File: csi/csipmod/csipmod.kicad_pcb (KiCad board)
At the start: 2 copper layers, 48 x 50 mm, 38 parts, among them J1 PMOD_1A, J2 PMOD_1B, P1 PICAM, U1 LD3985M18R_SOT23, U2 PCA9306

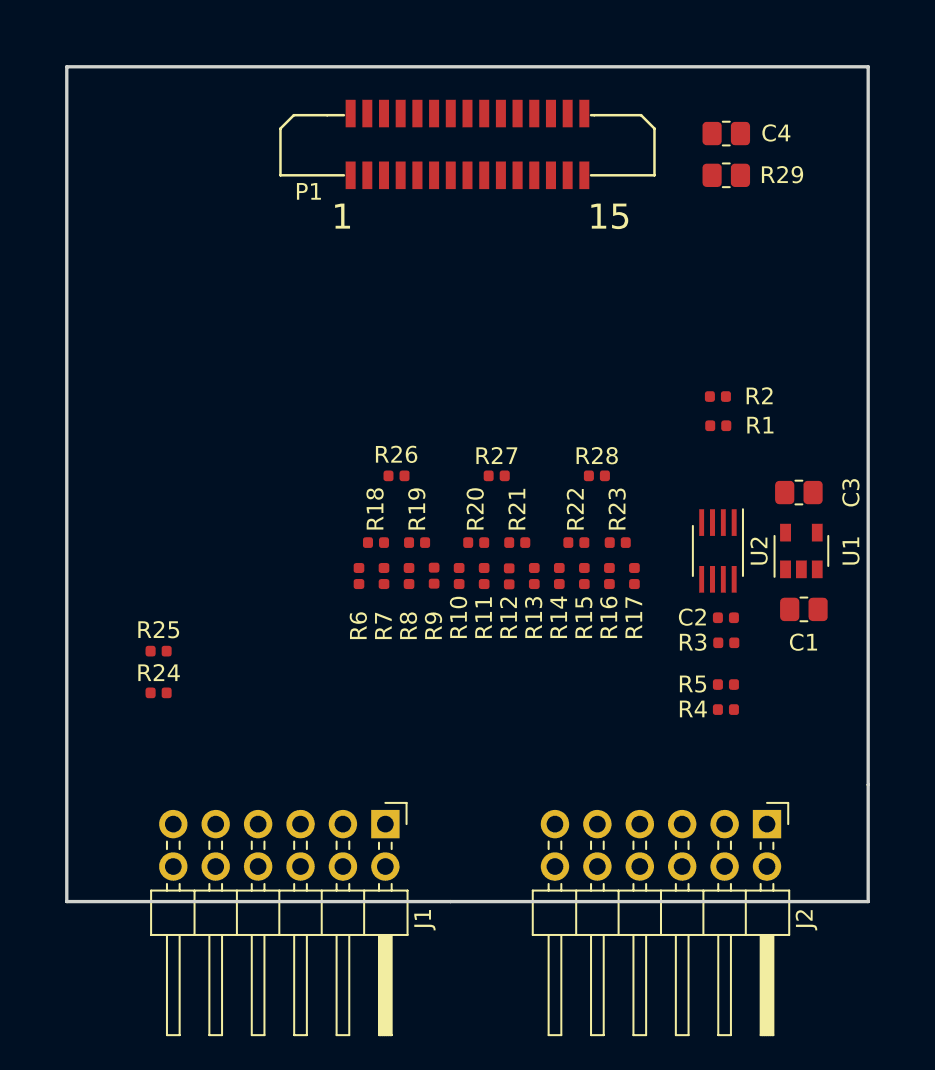
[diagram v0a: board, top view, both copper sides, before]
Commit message: csipmod: Routed
Signed-off-by: David Shah <davey1576@gmail.com>
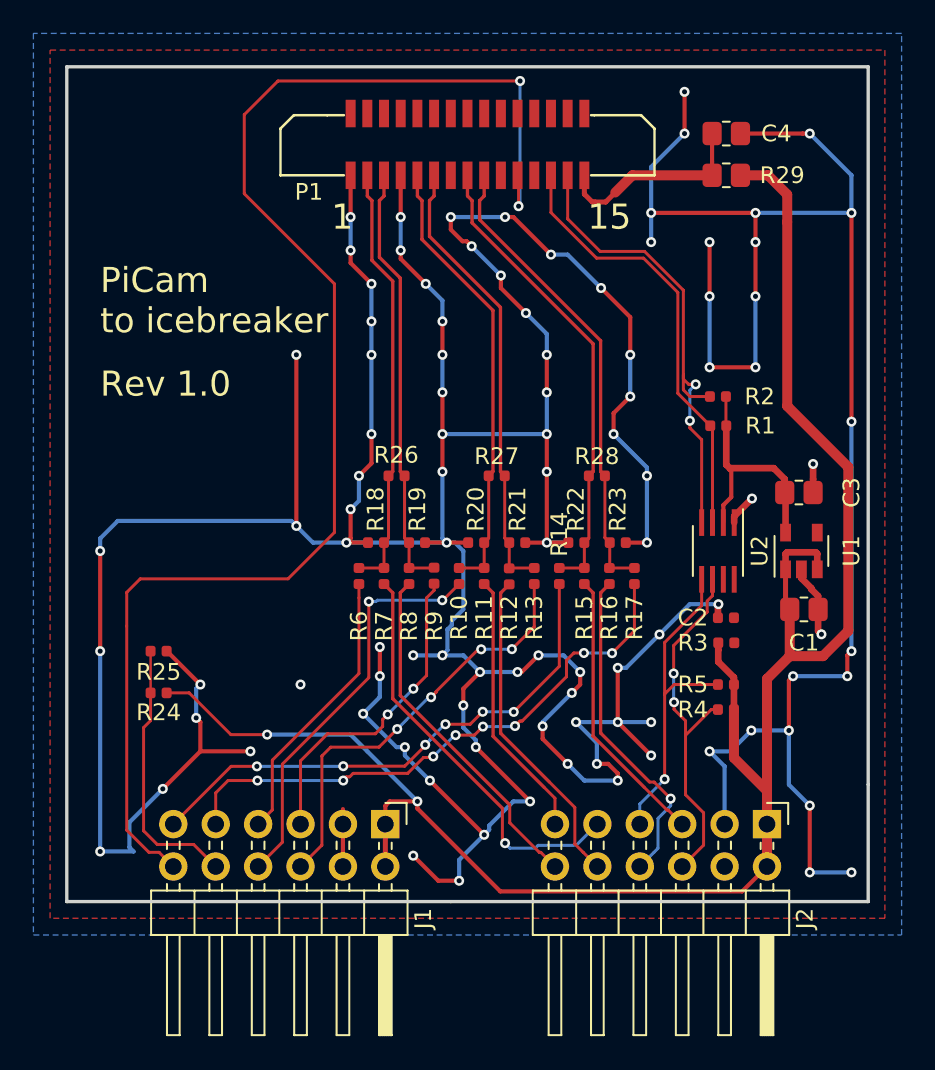
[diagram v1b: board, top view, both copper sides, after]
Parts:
- turned R14 to 270 degrees
- turned R24 to 180 degrees
- turned R25 to 0 degrees
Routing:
- net GND: track 0.00 -> 404.0 mm, vias 0 -> 100
- net +3V3: track 0.00 -> 115.3 mm, vias 0 -> 2
- net /CAM_ENABLE: track 0.00 -> 85.9 mm, vias 0 -> 2
- net /LPCLK+: track 0.00 -> 34.4 mm, vias 0 -> 8
- net /LPCLK-: track 0.00 -> 32.0 mm, vias 0 -> 6
- net /CAM_SDA: track 0.00 -> 28.9 mm, vias 0 -> 2
- net /CCLK+: track 0.00 -> 28.4 mm
- net /CCLK-: track 0.00 -> 28.4 mm
- net /CD1+: track 0.00 -> 27.1 mm
- net /CD1-: track 0.00 -> 27.1 mm
- net /CAM_SCL: track 0.00 -> 26.5 mm
- net /CD0+: track 0.00 -> 25.9 mm
- net /CD0-: track 0.00 -> 25.9 mm
- net /LPD1+: track 0.00 -> 25.7 mm, vias 0 -> 4
- net /HSD0-: track 0.00 -> 24.8 mm, vias 0 -> 1
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- added copper zone on B.Cu, net GND
- added copper zone on F.Cu, net GND
- added copper zone on In1.Cu, net GND
- added copper zone on In2.Cu, net GND
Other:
- copper layers 2 -> 4
- net class Default: clearance 0.2 -> 0.15; trace_width 0.25 -> 0.15; via_dia 0.8 -> 0.6; via_drill 0.4 -> 0.3
- rule trace_clearance: 0.2 -> 0.15
- rule trace_min: 0.2 -> 0.15
- rule via_min_size: 0.4 -> 0.16
- board text added: "PiCam to icebreaker"
- board text added: "Rev 1.0"

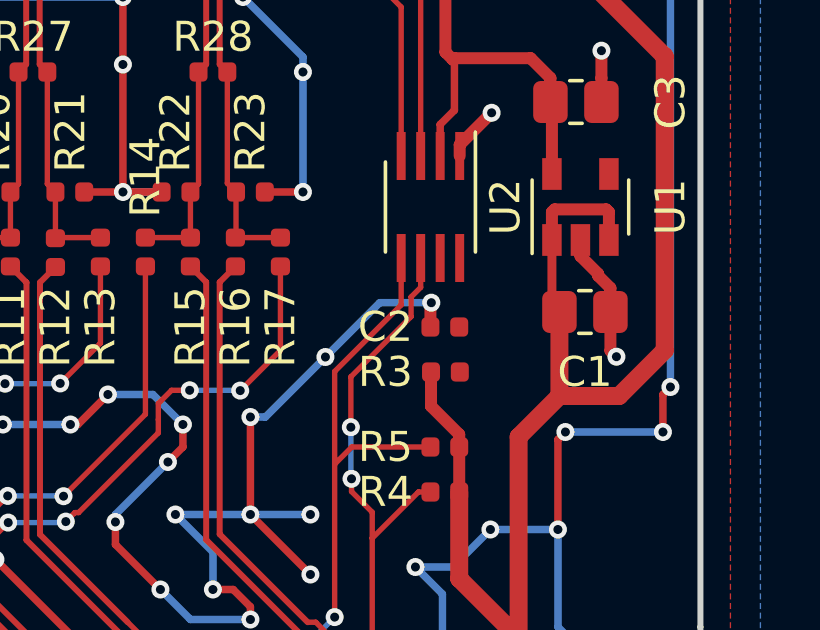
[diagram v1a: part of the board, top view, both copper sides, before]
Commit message: Adding CSI schematic and gerbers
Signed-off-by: David Shah <davey1576@gmail.com>
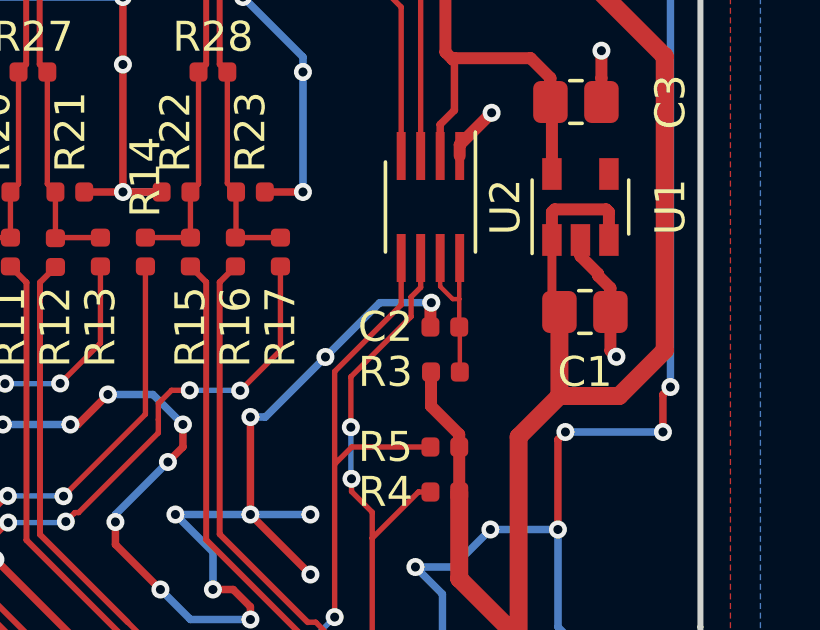
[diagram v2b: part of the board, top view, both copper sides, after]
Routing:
- net Net-(C2-Pad1): track 0.00 -> 5.57 mm
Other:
- rule pad_to_mask_clearance: 0.2 -> 0
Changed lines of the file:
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@@
     (thickness 1.6)
     (drawings 10)
-    (tracks 658)
+    (tracks 666)
     (zones 0)
     (modules 38)
@@
   )
   (setup
-    (last_trace_width 0.25)
+    (last_trace_width 0.15)
     (user_trace_width 0.15)
     (user_trace_width 0.18)
@@
     (pad_size 1.524 1.524)
     (pad_drill 0.762)
-    (pad_to_mask_clearance 0.2)
+    (pad_to_mask_clearance 0)
     (aux_axis_origin 0 0)
     (visible_elements FFFDFF7F)
     (pcbplotparams
-      (layerselection 0x010fc_ffffffff)
-      (usegerberextensions false)
+      (layerselection 0x010f0_ffffffff)
+      (usegerberextensions true)
       (usegerberattributes false)
       (usegerberadvancedattributes false)
@@
       (psa4output false)
       (plotreference true)
-      (plotvalue true)
+      (plotvalue false)
       (plotinvisibletext false)
       (padsonsilk false)
@@
       (outputformat 1)
       (mirror false)
-      (drillshape 1)
+      (drillshape 0)
       (scaleselection 1)
-      (outputdirectory ""))
+      (outputdirectory "csipmod-gerber"))
   )
   (net 0 "")
@@
   (via (at 148 82.25) (size 0.6) (drill 0.3) (layers F.Cu B.Cu) (net 4))
   (segment (start 146 80.25) (end 148 82.25) (width 0.25) (layer F.Cu) (net 4))
-  (via (at 135.75 69.5) (size 0.6) (drill 0.3) (layers F.Cu B.Cu) (net 4) (status 1000000))
-  (segment (start 136.065001 74.184999) (end 136.75 73.5) (width 0.25) (layer B.Cu) (net 4) (status 1000000))
-  (segment (start 135.75 69.5) (end 129.75 69.5) (width 0.25) (layer B.Cu) (net 4) (status 1000000))
-  (via (at 129.75 69.5) (size 0.6) (drill 0.3) (layers F.Cu B.Cu) (net 4) (status 1000000))
-  (segment (start 135.5 76.25) (end 135.799999 75.950001) (width 0.25) (layer B.Cu) (net 4) (status 1000000))
-  (segment (start 135.799999 75.950001) (end 135.799999 74.700001) (width 0.25) (layer B.Cu) (net 4) (status 1000000))
-  (segment (start 136.75 73.5) (end 136.75 70) (width 0.25) (layer B.Cu) (net 4) (status 1000000))
-  (segment (start 135.799999 74.700001) (end 136.065001 74.434999) (width 0.25) (layer B.Cu) (net 4) (status 1000000))
-  (segment (start 136.75 70) (end 136.25 69.5) (width 0.25) (layer B.Cu) (net 4) (status 1000000))
-  (segment (start 136.065001 74.434999) (end 136.065001 74.184999) (width 0.25) (layer B.Cu) (net 4) (status 1000000))
-  (segment (start 136.25 69.5) (end 135.75 69.5) (width 0.25) (layer B.Cu) (net 4) (status 1000000))
-  (via (at 135.5 76.25) (size 0.6) (drill 0.3) (layers F.Cu B.Cu) (net 4) (status 1000000))
+  (via (at 135.75 69.5) (size 0.6) (drill 0.3) (layers F.Cu B.Cu) (net 4))
+  (segment (start 136.065001 74.184999) (end 136.75 73.5) (width 0.25) (layer B.Cu) (net 4))
+  (segment (start 135.75 69.5) (end 129.75 69.5) (width 0.25) (layer B.Cu) (net 4))
+  (via (at 129.75 69.5) (size 0.6) (drill 0.3) (layers F.Cu B.Cu) (net 4))
+  (segment (start 135.5 76.25) (end 135.799999 75.950001) (width 0.25) (layer B.Cu) (net 4))
+  (segment (start 135.799999 75.950001) (end 135.799999 74.700001) (width 0.25) (layer B.Cu) (net 4))
+  (segment (start 136.75 73.5) (end 136.75 70) (width 0.25) (layer B.Cu) (net 4))
+  (segment (start 135.799999 74.700001) (end 136.065001 74.434999) (width 0.25) (layer B.Cu) (net 4))
+  (segment (start 136.75 70) (end 136.25 69.5) (width 0.25) (layer B.Cu) (net 4))
+  (segment (start 136.065001 74.434999) (end 136.065001 74.184999) (width 0.25) (layer B.Cu) (net 4))
+  (segment (start 136.25 69.5) (end 135.75 69.5) (width 0.25) (layer B.Cu) (net 4))
+  (via (at 135.5 76.25) (size 0.6) (drill 0.3) (layers F.Cu B.Cu) (net 4))
   (segment (start 129.75 69.5) (end 131.04 69.5) (width 0.25) (layer F.Cu) (net 4))
   (segment (start 134.46 69.5) (end 135.75 69.5) (width 0.25) (layer F.Cu) (net 4))
@@
   (segment (start 149.93001 60.35001) (end 149.93001 59.46) (width 0.18) (layer F.Cu) (net 7))
   (segment (start 149.93001 59.46) (end 149.93001 54.383306) (width 0.18) (layer F.Cu) (net 7))
+  (segment (start 152.98 75.5) (end 152.98 74.02) (width 0.15) (layer F.Cu) (net 8) (status C00000))
+  (segment (start 152.98 74.02) (end 152.96 74) (width 0.15) (layer F.Cu) (net 8) (status C00000))
+  (segment (start 152.96 71.715) (end 152.975 71.7) (width 0.15) (layer F.Cu) (net 8) (status C00000))
+  (segment (start 152.745 73.07) (end 152.96 73.07) (width 0.15) (layer F.Cu) (net 8))
+  (segment (start 152.325 72.65) (end 152.745 73.07) (width 0.15) (layer F.Cu) (net 8))
+  (segment (start 152.325 71.7) (end 152.325 72.65) (width 0.15) (layer F.Cu) (net 8))
+  (segment (start 152.96 74) (end 152.96 73.07) (width 0.15) (layer F.Cu) (net 8))
+  (segment (start 152.96 73.07) (end 152.96 71.715) (width 0.15) (layer F.Cu) (net 8))
   (segment (start 151.6 79.5) (end 150.06 81.04) (width 0.18) (layer F.Cu) (net 9))
   (segment (start 152 79.5) (end 151.6 79.5) (width 0.18) (layer F.Cu) (net 9))
